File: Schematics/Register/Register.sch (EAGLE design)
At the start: 23 parts

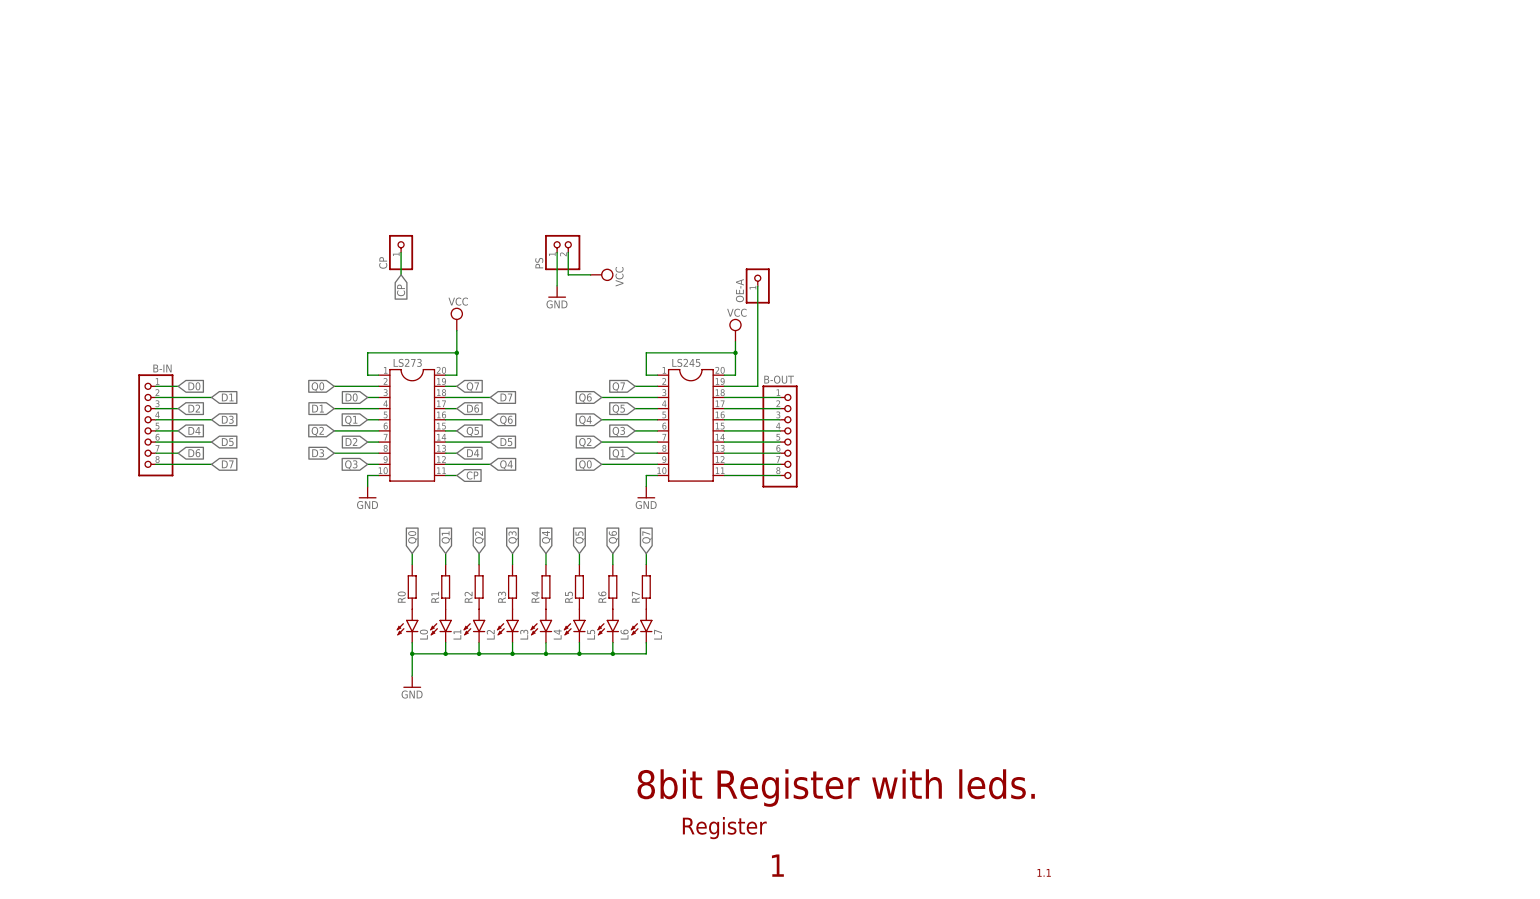
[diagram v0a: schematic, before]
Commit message: Register, PC, RAM will be solid board not modules, brd is pretty simple.
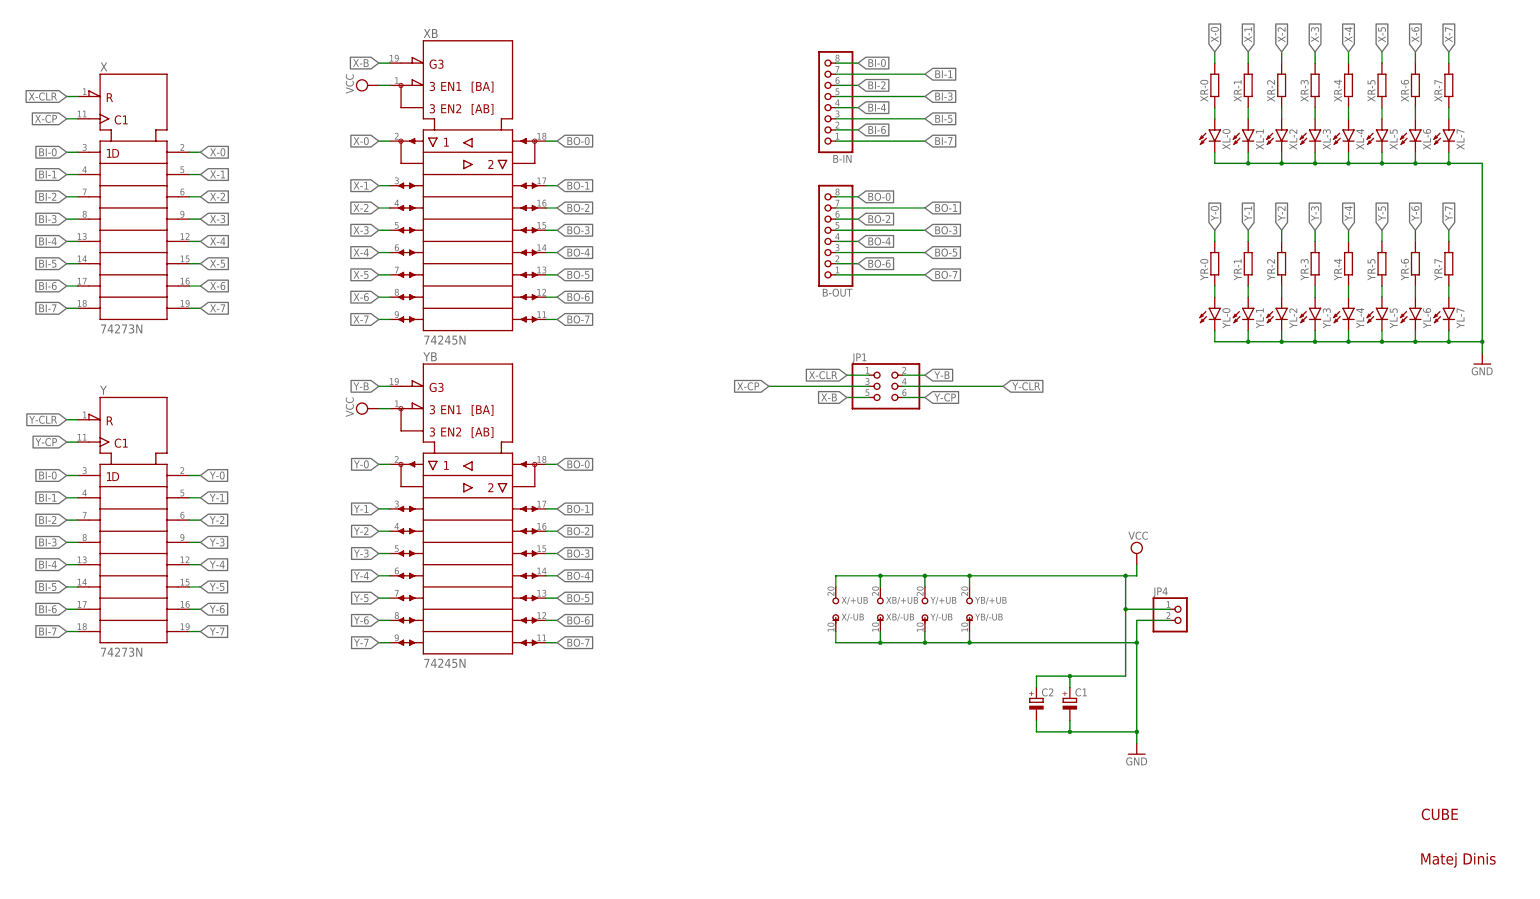
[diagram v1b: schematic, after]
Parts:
- removed CP, OE-A: (no value), pinhead:PINHD-1X1
- removed L0, L1, L2, L3, L4, L5, L6, L7: (no value), led:LED5MM
- removed LS245, LS273: (no value), ic-package:DIL20S
- removed PS: (no value), pinhead:PINHD-1X2
- removed R0, R1, R2, R3, R4, R5, R6, R7: (no value), rcl:R-EU_0204/7
- added C1, C2: (no value), rcl:CPOL-EUE3.5-8
- added JP1: (no value), pinhead:PINHD-2X3
- added JP4: (no value), pinhead:PINHD-1X2
- added X, Y: 74273N, 74ttl-din:74273N
- added XB, YB: 74245N, 74ttl-din:74245N
- added XL-0, XL-1, XL-2, XL-3, XL-4, XL-5, XL-6, XL-7, YL-0, YL-1, YL-2, YL-3, YL-4, YL-5, YL-6, YL-7: (no value), led:LED5MM
- added XR-0, XR-1, XR-2, XR-3, XR-4, XR-5, XR-6, XR-7, YR-0, YR-1, YR-2, YR-3, YR-4, YR-5, YR-6, YR-7: (no value), rcl:R-EU_0207/10
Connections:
- removed net BO0: B-OUT.8, LS245.11
- removed net BO1: B-OUT.7, LS245.12
- removed net BO2: B-OUT.6, LS245.13
- removed net BO3: B-OUT.5, LS245.14
- removed net BO4: B-OUT.4, LS245.15
- removed net BO5: B-OUT.3, LS245.16
- removed net BO6: B-OUT.2, LS245.17
- removed net BO7: B-OUT.1, LS245.18
- removed net CP: CP.1, LS273.11
- removed net D0: B-IN.1, LS273.3
- removed net D1: B-IN.2, LS273.4
- removed net D2: B-IN.3, LS273.7
- removed net D3: B-IN.4, LS273.8
- removed net D4: B-IN.5, LS273.13
- removed net D5: B-IN.6, LS273.14
- removed net D6: B-IN.7, LS273.17
- removed net D7: B-IN.8, LS273.18
- removed net N$1: L7.A, R7.1
- removed net N$10: L1.A, R1.1
- removed net N$11: L0.A, R0.1
- removed net N$18: LS245.19, OE-A.1
- removed net N$5: L6.A, R6.1
- removed net N$6: L5.A, R5.1
- removed net N$7: L4.A, R4.1
- removed net N$8: L3.A, R3.1
- removed net N$9: L2.A, R2.1
- removed net Q0: LS245.9, LS273.2, R0.2
- removed net Q1: LS245.8, LS273.5, R1.2
- removed net Q2: LS245.7, LS273.6, R2.2
- removed net Q3: LS245.6, LS273.9, R3.2
- removed net Q4: LS245.5, LS273.12, R4.2
- removed net Q5: LS245.4, LS273.15, R5.2
- removed net Q6: LS245.3, LS273.16, R6.2
- removed net Q7: LS245.2, LS273.19, R7.2
- new net BI-0: B-IN.8, X1.1D, Y1.1D
- new net BI-1: B-IN.7, X1.2D, Y1.2D
- new net BI-2: B-IN.6, X1.3D, Y1.3D
- new net BI-3: B-IN.5, X1.4D, Y1.4D
- new net BI-4: B-IN.4, X1.5D, Y1.5D
- new net BI-5: B-IN.3, X1.6D, Y1.6D
- new net BI-6: B-IN.2, X1.7D, Y1.7D
- new net BI-7: B-IN.1, X1.8D, Y1.8D
- new net BO-0: B-OUT.8, XB1.B1, YB1.B1
- new net BO-1: B-OUT.7, XB1.B2, YB1.B2
- new net BO-2: B-OUT.6, XB1.B3, YB1.B3
- new net BO-3: B-OUT.5, XB1.B4, YB1.B4
- new net BO-4: B-OUT.4, XB1.B5, YB1.B5
- new net BO-5: B-OUT.3, XB1.B6, YB1.B6
- new net BO-6: B-OUT.2, XB1.B7, YB1.B7
- new net BO-7: B-OUT.1, XB1.B8, YB1.B8
- new net N$113: XL-1.A, XR-1.1
- new net N$116: XL-2.A, XR-2.1
- new net N$119: XL-3.A, XR-3.1
- new net N$122: XL-4.A, XR-4.1
- new net N$125: XL-5.A, XR-5.1
- new net N$128: XL-6.A, XR-6.1
- new net N$131: XL-7.A, XR-7.1
- new net N$134: YL-0.A, YR-0.1
- new net N$137: YL-1.A, YR-1.1
- new net N$140: YL-2.A, YR-2.1
- new net N$143: YL-3.A, YR-3.1
- new net N$146: YL-4.A, YR-4.1
- new net N$149: YL-5.A, YR-5.1
- new net N$152: YL-6.A, YR-6.1
- new net N$155: YL-7.A, YR-7.1
- new net N$2: XL-0.A, XR-0.1
- new net X-0: X1.1Q, XB1.A1, XR-0.2
- new net X-1: X1.2Q, XB1.A2, XR-1.2
- new net X-2: X1.3Q, XB1.A3, XR-2.2
- new net X-3: X1.4Q, XB1.A4, XR-3.2
- new net X-4: X1.5Q, XB1.A5, XR-4.2
- new net X-5: X1.6Q, XB1.A6, XR-5.2
- new net X-6: X1.7Q, XB1.A7, XR-6.2
- new net X-7: X1.8Q, XB1.A8, XR-7.2
- new net X-B: JP1.5, XB1.!G
- new net X-CLR: JP1.1, X1.!CLR
- new net X-CP: JP1.3, X1.CLK
- new net Y-0: Y1.1Q, YB1.A1, YR-0.2
- new net Y-1: Y1.2Q, YB1.A2, YR-1.2
- new net Y-2: Y1.3Q, YB1.A3, YR-2.2
- new net Y-3: Y1.4Q, YB1.A4, YR-3.2
- new net Y-4: Y1.5Q, YB1.A5, YR-4.2
- new net Y-5: Y1.6Q, YB1.A6, YR-5.2
- new net Y-6: Y1.7Q, YB1.A7, YR-6.2
- new net Y-7: Y1.8Q, YB1.A8, YR-7.2
- new net Y-B: JP1.2, YB1.!G
- new net Y-CLR: JP1.4, Y1.!CLR
- new net Y-CP: JP1.6, Y1.CLK
- net GND: now also C1.-, C2.-, JP4.2, X/-UB.-UB, XB/-UB.-UB, XL-0.C, XL-1.C, XL-2.C, XL-3.C, XL-4.C, XL-5.C, XL-6.C, XL-7.C, Y/-UB.-UB, YB/-UB.-UB, YL-0.C, YL-1.C, YL-2.C, YL-3.C, YL-4.C, YL-5.C, YL-6.C, YL-7.C; no longer L0.C, L1.C, L2.C, L3.C, L4.C, L5.C, L6.C, L7.C, LS245.10, LS273.10, PS.1
- net VCC: now also C1.+, C2.+, JP4.1, X/+UB.+UB, XB/+UB.+UB, XB1.DIR, Y/+UB.+UB, YB/+UB.+UB, YB1.DIR; no longer LS245.1, LS245.20, LS273.1, LS273.20, PS.2
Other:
- note added: "CUBE"
- note added: "Matej Dinis"
- note removed: "1"
- note removed: "1.1"
- note removed: "8bit Register with leds."
- note removed: "Register"
- moved on the sheet: B-IN, B-OUT

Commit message: Added register.
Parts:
- removed C1, C2: (no value), rcl:CPOL-EUE3.5-8
- removed JP1: (no value), pinhead:PINHD-2X3
- removed JP4: (no value), pinhead:PINHD-1X2
- removed X, Y: 74273N, 74ttl-din:74273N
- removed XB, YB: 74245N, 74ttl-din:74245N
- removed XL-0, XL-1, XL-2, XL-3, XL-4, XL-5, XL-6, XL-7, YL-0, YL-1, YL-2, YL-3, YL-4, YL-5, YL-6, YL-7: (no value), led:LED5MM
- removed XR-0, XR-1, XR-2, XR-3, XR-4, XR-5, XR-6, XR-7, YR-0, YR-1, YR-2, YR-3, YR-4, YR-5, YR-6, YR-7: (no value), rcl:R-EU_0207/10
- added CP, OE-A: (no value), pinhead:PINHD-1X1
- added L0, L1, L2, L3, L4, L5, L6, L7: (no value), led:LED5MM
- added LS245, LS273: (no value), ic-package:DIL20S
- added PS: (no value), pinhead:PINHD-1X2
- added R0, R1, R2, R3, R4, R5, R6, R7: (no value), rcl:R-EU_0204/7
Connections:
- removed net BI-0: B-IN.8, X1.1D, Y1.1D
- removed net BI-1: B-IN.7, X1.2D, Y1.2D
- removed net BI-2: B-IN.6, X1.3D, Y1.3D
- removed net BI-3: B-IN.5, X1.4D, Y1.4D
- removed net BI-4: B-IN.4, X1.5D, Y1.5D
- removed net BI-5: B-IN.3, X1.6D, Y1.6D
- removed net BI-6: B-IN.2, X1.7D, Y1.7D
- removed net BI-7: B-IN.1, X1.8D, Y1.8D
- removed net BO-0: B-OUT.8, XB1.B1, YB1.B1
- removed net BO-1: B-OUT.7, XB1.B2, YB1.B2
- removed net BO-2: B-OUT.6, XB1.B3, YB1.B3
- removed net BO-3: B-OUT.5, XB1.B4, YB1.B4
- removed net BO-4: B-OUT.4, XB1.B5, YB1.B5
- removed net BO-5: B-OUT.3, XB1.B6, YB1.B6
- removed net BO-6: B-OUT.2, XB1.B7, YB1.B7
- removed net BO-7: B-OUT.1, XB1.B8, YB1.B8
- removed net N$113: XL-1.A, XR-1.1
- removed net N$116: XL-2.A, XR-2.1
- removed net N$119: XL-3.A, XR-3.1
- removed net N$122: XL-4.A, XR-4.1
- removed net N$125: XL-5.A, XR-5.1
- removed net N$128: XL-6.A, XR-6.1
- removed net N$131: XL-7.A, XR-7.1
- removed net N$134: YL-0.A, YR-0.1
- removed net N$137: YL-1.A, YR-1.1
- removed net N$140: YL-2.A, YR-2.1
- removed net N$143: YL-3.A, YR-3.1
- removed net N$146: YL-4.A, YR-4.1
- removed net N$149: YL-5.A, YR-5.1
- removed net N$152: YL-6.A, YR-6.1
- removed net N$155: YL-7.A, YR-7.1
- removed net N$2: XL-0.A, XR-0.1
- removed net X-0: X1.1Q, XB1.A1, XR-0.2
- removed net X-1: X1.2Q, XB1.A2, XR-1.2
- removed net X-2: X1.3Q, XB1.A3, XR-2.2
- removed net X-3: X1.4Q, XB1.A4, XR-3.2
- removed net X-4: X1.5Q, XB1.A5, XR-4.2
- removed net X-5: X1.6Q, XB1.A6, XR-5.2
- removed net X-6: X1.7Q, XB1.A7, XR-6.2
- removed net X-7: X1.8Q, XB1.A8, XR-7.2
- removed net X-B: JP1.5, XB1.!G
- removed net X-CLR: JP1.1, X1.!CLR
- removed net X-CP: JP1.3, X1.CLK
- removed net Y-0: Y1.1Q, YB1.A1, YR-0.2
- removed net Y-1: Y1.2Q, YB1.A2, YR-1.2
- removed net Y-2: Y1.3Q, YB1.A3, YR-2.2
- removed net Y-3: Y1.4Q, YB1.A4, YR-3.2
- removed net Y-4: Y1.5Q, YB1.A5, YR-4.2
- removed net Y-5: Y1.6Q, YB1.A6, YR-5.2
- removed net Y-6: Y1.7Q, YB1.A7, YR-6.2
- removed net Y-7: Y1.8Q, YB1.A8, YR-7.2
- removed net Y-B: JP1.2, YB1.!G
- removed net Y-CLR: JP1.4, Y1.!CLR
- removed net Y-CP: JP1.6, Y1.CLK
- new net BO0: B-OUT.8, LS245.11
- new net BO1: B-OUT.7, LS245.12
- new net BO2: B-OUT.6, LS245.13
- new net BO3: B-OUT.5, LS245.14
- new net BO4: B-OUT.4, LS245.15
- new net BO5: B-OUT.3, LS245.16
- new net BO6: B-OUT.2, LS245.17
- new net BO7: B-OUT.1, LS245.18
- new net CP: CP.1, LS273.11
- new net D0: B-IN.1, LS273.3
- new net D1: B-IN.2, LS273.4
- new net D2: B-IN.3, LS273.7
- new net D3: B-IN.4, LS273.8
- new net D4: B-IN.5, LS273.13
- new net D5: B-IN.6, LS273.14
- new net D6: B-IN.7, LS273.17
- new net D7: B-IN.8, LS273.18
- new net N$1: L7.A, R7.1
- new net N$10: L1.A, R1.1
- new net N$11: L0.A, R0.1
- new net N$18: LS245.19, OE-A.1
- new net N$5: L6.A, R6.1
- new net N$6: L5.A, R5.1
- new net N$7: L4.A, R4.1
- new net N$8: L3.A, R3.1
- new net N$9: L2.A, R2.1
- new net Q0: LS245.9, LS273.2, R0.2
- new net Q1: LS245.8, LS273.5, R1.2
- new net Q2: LS245.7, LS273.6, R2.2
- new net Q3: LS245.6, LS273.9, R3.2
- new net Q4: LS245.5, LS273.12, R4.2
- new net Q5: LS245.4, LS273.15, R5.2
- new net Q6: LS245.3, LS273.16, R6.2
- new net Q7: LS245.2, LS273.19, R7.2
- net GND: now also L0.C, L1.C, L2.C, L3.C, L4.C, L5.C, L6.C, L7.C, LS245.10, LS273.10, PS.1; no longer C1.-, C2.-, JP4.2, X/-UB.-UB, XB/-UB.-UB, XL-0.C, XL-1.C, XL-2.C, XL-3.C, XL-4.C, XL-5.C, XL-6.C, XL-7.C, Y/-UB.-UB, YB/-UB.-UB, YL-0.C, YL-1.C, YL-2.C, YL-3.C, YL-4.C, YL-5.C, YL-6.C, YL-7.C
- net VCC: now also LS245.1, LS245.20, LS273.1, LS273.20, PS.2; no longer C1.+, C2.+, JP4.1, X/+UB.+UB, XB/+UB.+UB, XB1.DIR, Y/+UB.+UB, YB/+UB.+UB, YB1.DIR
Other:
- note added: "1"
- note added: "1.1"
- note added: "8bit Register with leds."
- note added: "Register"
- note removed: "CUBE"
- note removed: "Matej Dinis"
- moved on the sheet: B-IN, B-OUT
